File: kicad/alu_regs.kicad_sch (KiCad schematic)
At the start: 10 parts, among them U19 SN74F377AN, U20 SN74F377AN, U21 SN74F377AN, U5 ATF22V10C-7PX, U6 ATF22V10C-7PX

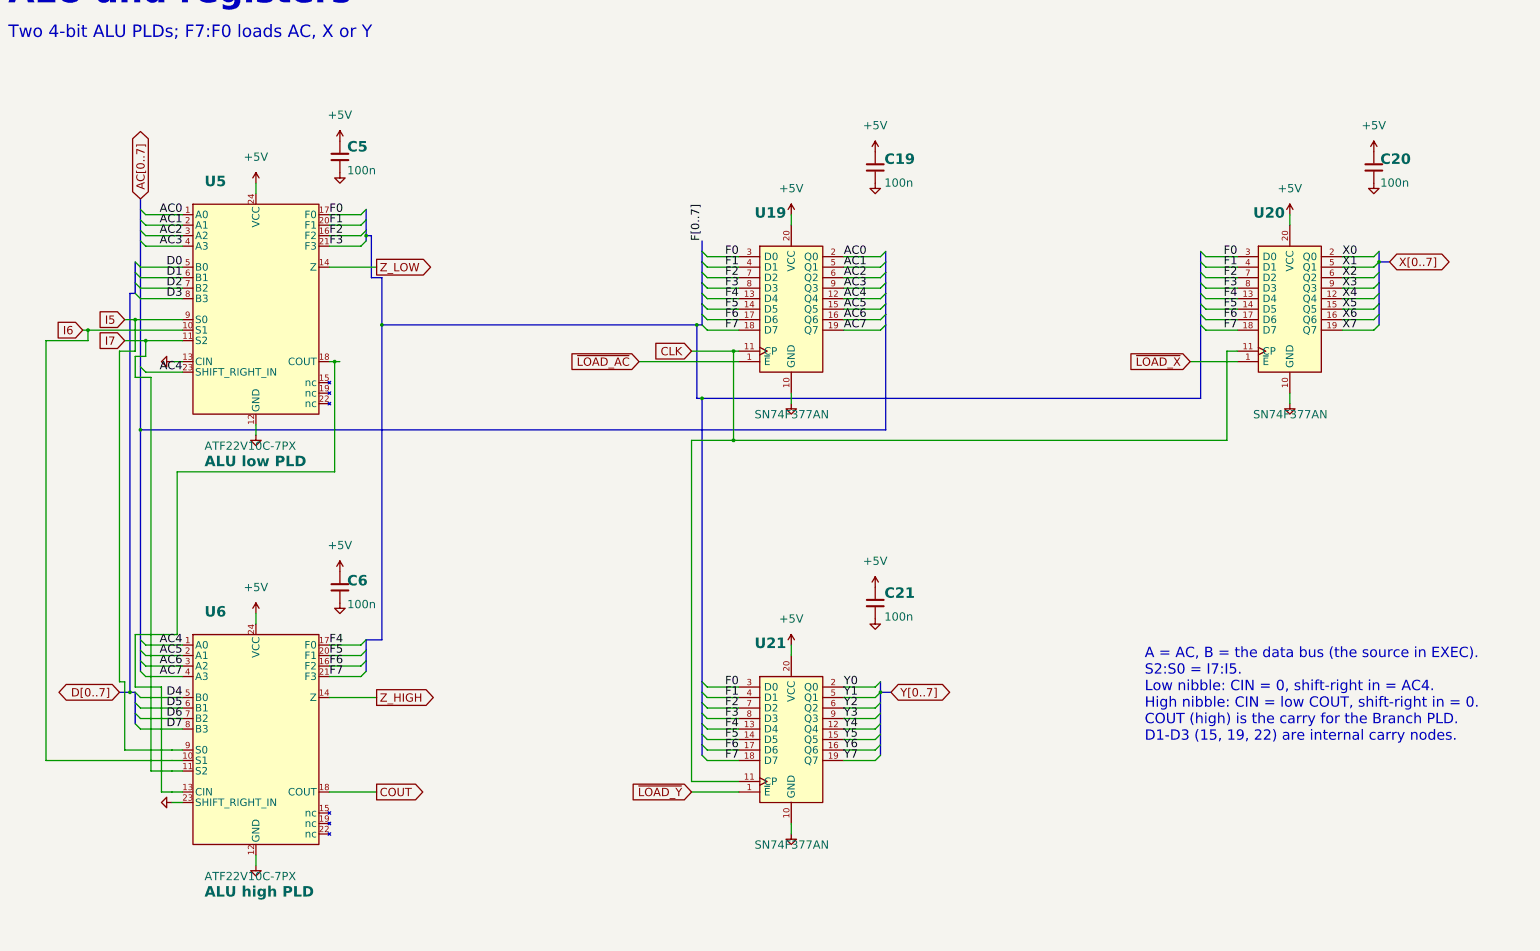
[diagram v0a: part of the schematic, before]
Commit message: Tidy every schematic sheet: spread parts, straight runs, buses kept, horizontal tabs
Shared port, expansion and cartridge sheets laid out by hand; buses from
other sheets get a bus label at each chip, busy control nets a label at
each pin; some PLD and connector symbols reordered so wires run straight;
sideways power symbols read across. 0 netlist problems, no overlaps.

Co-Authored-By: Claude Opus 5.5 (1M context) <noreply@anthropic.com>
Claude-Session: https://claude.ai/code/session_01L9AkLuEg13EebxDmgXsaEp
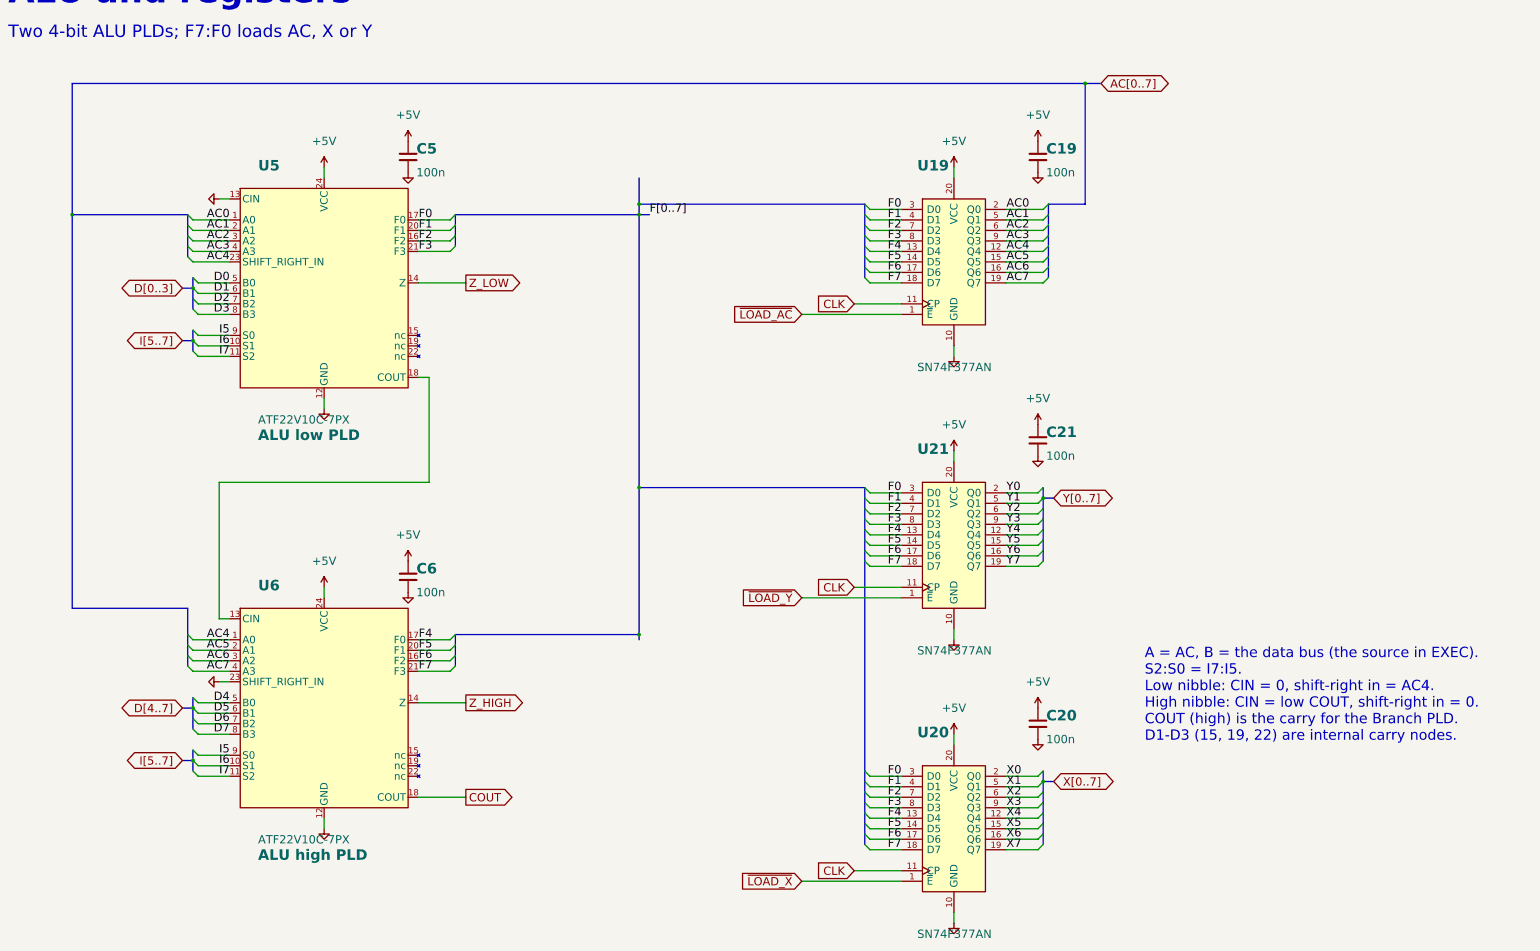
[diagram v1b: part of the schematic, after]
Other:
- moved on the sheet: C5, C6, U5, U6

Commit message: Bill of materials for the main board, cartridge and keyboard
Manufacturer and MPN fields on every schematic part (empty where none is
chosen), set from an MPN table in gen_kicad_schematic.py; net tie, cartridge
edge fingers and solder jumper excluded from the BOM.  gen_bom.py groups the
parts by part number into docs/BOM.md and docs/BOM.csv, adding sockets,
shunts, keyboard LEDs, keycaps, stabilizers and the keyboard ribbon cable.

Co-Authored-By: Claude Opus 5.5 (1M context) <noreply@anthropic.com>
Claude-Session: https://claude.ai/code/session_018iEnPngycbxX6Tt4Wzp3zN
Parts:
- U19, U20, U21: MPN (none) -> SN74F377AN; Manufacturer (none) -> Texas Instruments
- U5, U6: MPN (none) -> ATF22V10C-7PX; Manufacturer (none) -> Microchip

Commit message: Part numbers for the remaining parts; J6 Tensility 54-00174; optional J1 and J9-J12
Every schematic part gets Manufacturer/MPN: Yageo MFR-25 resistors by value,
Bourns 4609X networks, KEMET/TDK ceramics, Panasonic FR electrolytics, ECS
oscillator, Assmann VGA, Sullins headers, Wurth box header, Cherry switches.
Sockets get On Shore numbers (0.3" 24/28-pin are ED241DT/ED281DT; ED28DT is
0.6"). J6 becomes the Tensility 54-00174 TRRS jack with a footprint drawn
from its datasheet. Digi-Key prices from Justin for the oscillator, VGA and
audio jack. The expansion slot sockets and the keyboard header are optional,
with a BOM total without them.

Co-Authored-By: Claude Opus 5.5 (1M context) <noreply@anthropic.com>
Claude-Session: https://claude.ai/code/session_01L9AkLuEg13EebxDmgXsaEp
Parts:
- C19, C20, C21, C5, C6: MPN (none) -> C320C104K5R5TA; Manufacturer (none) -> KEMET

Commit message: Kit footprints: DIP sockets with puller room and part number, resistors with value
Justin: put the chip-puller room in the socket footprints (User.Eco1,
2.5 mm past each end) and the part number in silkscreen between the pin
rows; resistors get their value in silkscreen on the body. New
gen_kicad_kit_footprints.py derives them from KiCad's stock footprints;
schematic, symbols, BOM and PDFs now name them. The board file is left
as is (Justin is editing it): Update PCB from Schematic swaps them in.

Co-Authored-By: Claude Opus 5.5 (1M context) <noreply@anthropic.com>
Claude-Session: https://claude.ai/code/session_01JnVuvUvdWezUUU6Sgmg16H
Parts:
- U19, U20, U21: footprint Package_DIP:DIP-20_W7.62mm -> placard:DIP-20_W7.62mm_Socket_Puller
- U5, U6: footprint Package_DIP:DIP-24_W7.62mm -> placard:DIP-24_W7.62mm_Socket_Puller
